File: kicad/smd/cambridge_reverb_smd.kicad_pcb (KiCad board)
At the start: 2 copper layers, 155 x 90 mm, 143 parts, among them IC1 TL072CP, IC2 TL072CP, Q1 MMBF5457, Q2 MMBF5457, T1 reuse / AnTek AS-0524, U1 LM317T

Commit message: SPICE parameter sweeps with committed results; tremolo LFO fix (errata #19); re-route
spice/: six ngspice sweeps next to the fixed-point checks, and run_all.sh now
saves every result table to spice/results/ (committed evidence):
- sweep_preamp_bias: Vd vs R_s for LO/TYP/HI JFET corners (datasheet Idss 1/3/5
  mA). The recovered 2.2k suits a HIGH-Idss part (8.8 V); a typical part wants
  ~1.0k (8.5 V); a 1 mA part cannot reach 8-9 V at any R_s -> errata #15 quantified
- sweep_tonestack: response over the whole pot travel (1 kHz -1.6..-3.3 dB while
  10 kHz falls 14 dB)
- sweep_lfo_speed_recovered: the recovered single-arm Wien LFO oscillates only for
  pot <= ~27k (5 % of travel) at 45-80 Hz, and not at all elsewhere
- sweep_lfo_speed: the fixed network, 10.6 Hz .. 0.60 Hz at constant 0.96 Vpp
- sweep_classa_bias: standing current / heat / THD vs bias (1.4 % -> 0.002 %,
  0.11 -> 0.85 A)
- sweep_pa_headroom: clean power vs rail, mains -10 %..+10 % = 8.9 / 11.7 / 14.8 W

Errata #19 (HIGH): the tremolo LFO did not work as recovered (Wien start condition
gain > 2 + R1/R2 fails with the speed pot in one arm). Built design: dual-gang
250k lin speed pot (one gang per arm, same panel hole), 15k floors, 1 uF timing
caps; POT_SPD_A/B in schematic + BOM = one part. tran_tremolo_lfo.cir aligned
(10.59 Hz at the fast end). Docs: errata, Part 1 s5, Part 2 note, Part 6b, BOM
cross-check, spice README (sweep tables), PCB-NOTES test-point row, README.

Both boards regenerated and re-routed (six settings each; Freerouting is
deterministic per input but placement-sensitive): THT 167/168, 3 starved-thermal
errors (was 166/166 clean); SMD 162/169, DRC clean (was 165/167 + 1 error).
Reports in kicad/reports/, open links listed in PCB-NOTES.

Co-Authored-By: Claude Fable 5.1 <noreply@anthropic.com>
Claude-Session: https://claude.ai/code/session_01Vk8HkvCugxFpQsBPVnNT2H
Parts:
- removed POT_SPD: 500k lin, WirePad_1x03_P2.54mm_D1.2mm
- removed R_lfo1: 33k, R_0805_2012Metric
- added POT_SPD_A: 250k lin dual, WirePad_1x03_P2.54mm_D1.2mm, F.Cu at (50.4, 81.5)
- added POT_SPD_B: 250k lin dual, WirePad_1x03_P2.54mm_D1.2mm, F.Cu at (59.8, 81.5)
- added R_lfo_sh: 15k, R_0805_2012Metric, F.Cu at (48.6, 51.1)
- C_lfo1, C_lfo2: value 100nF -> 1uF; footprint C_1206_3216Metric -> C_1210_3225Metric
- R_lfo_ser: value 10k -> 15k
- moved R_mrb_ser 25.8 mm to (76.0, 14.1)
- moved C_lfo1 16.7 mm to (39.1, 40.4)
- moved C_lfo2 15.8 mm to (33.9, 40.4)
- moved POT_REV 9.43 mm to (90.7, 81.5)
- moved POT_DPT 9.43 mm to (69.3, 81.5)
- moved FS1 9.43 mm to (100.1, 81.5)
- moved LS1 9.43 mm to (117.6, 81.5)
- moved REV1 9.43 mm to (78.7, 81.5)
- moved D_lfo2 5.25 mm to (27.9, 51.3)
- moved R_led 5.25 mm to (60.6, 51.1)
- moved R_lfo_fb1 5.25 mm to (52.6, 51.1)
- moved R_trem1 5.25 mm to (68.6, 51.1)
- moved R_vbt1 5.25 mm to (32.6, 51.1)
- moved R_vbt2 5.25 mm to (36.6, 51.1)
- moved D_lfo1 5.25 mm to (22.5, 51.3)
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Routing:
- net SPK_P: track 65.2 -> 173.9 mm, vias 2 -> 1
- net TONE_OUT: track 118.7 -> 202.0 mm, vias 2 -> 3
- net WMX: track 91.1 -> 159.4 mm, vias 4 -> 2
- net DRMX: track 52.5 -> 116.2 mm, vias 2 -> 4
- net +17V: track 327.0 -> 379.3 mm, vias 1 -> 2
- net LFO_N: track 57.2 -> 109.0 mm, vias 1 -> 3
- net Q2D: track 137.1 -> 94.3 mm, vias 2 -> 4
- net SPD_B: track 0.00 -> 37.4 mm, vias 0 -> 1
- net MRB_OUT: track 93.0 -> 57.1 mm, vias 0 -> 1
- net TREM_OUT: track 118.4 -> 89.0 mm
- net LFO_P: track 71.0 -> 99.0 mm, vias 5 -> 0
- net QRD: track 56.9 -> 84.4 mm, vias 4 -> 2
- net MRB_T: track 72.4 -> 97.3 mm, vias 0 -> 3
- net PREAMP_OUT: track 160.2 -> 135.6 mm
- net WN1: track 77.4 -> 56.4 mm, vias 4 -> 3
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
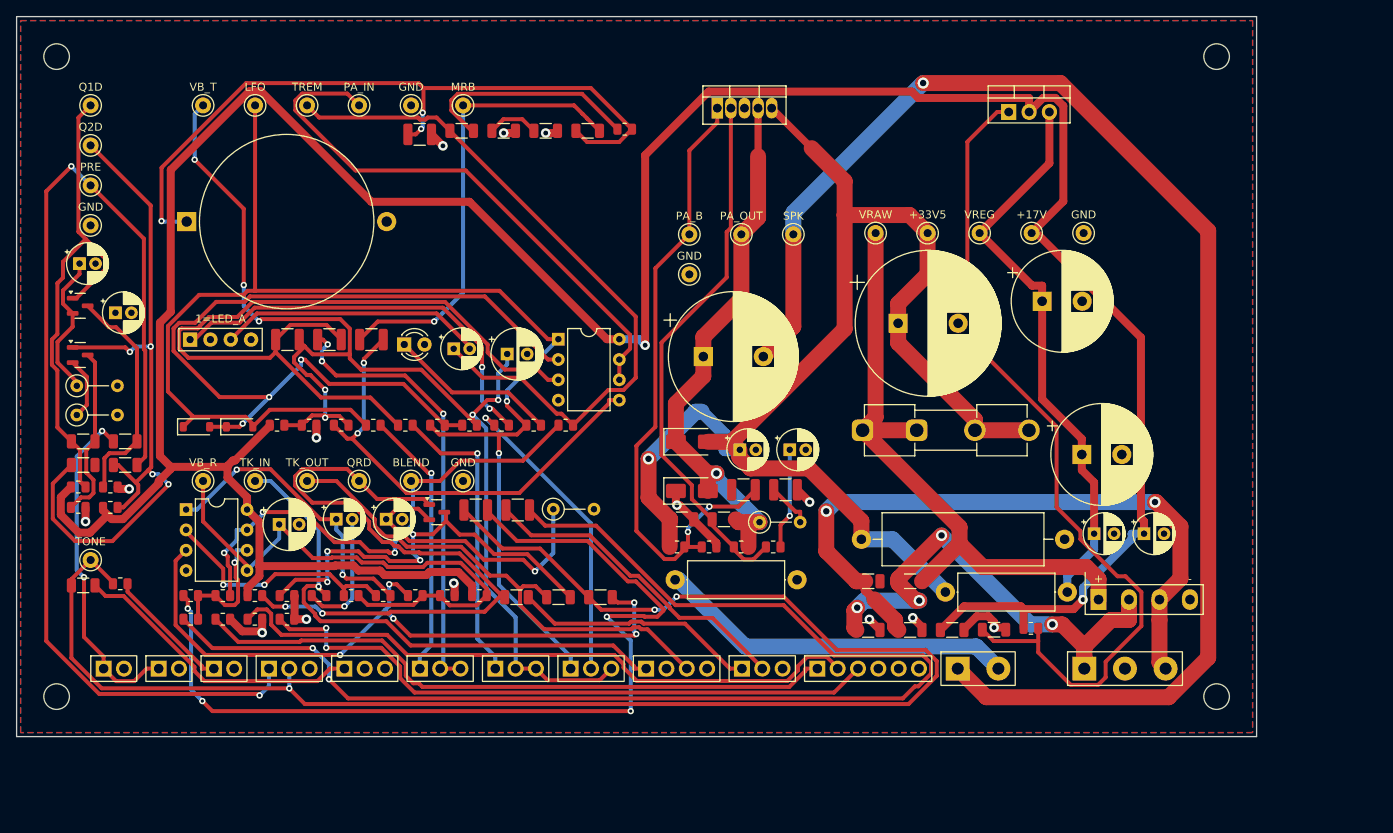
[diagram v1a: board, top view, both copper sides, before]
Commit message: Tone stack: Bass + Treble (passive James) with a switchable mid cut (errata #20)
The panel has Bass and Treble pots, but the design carried a single treble-cut
"Tone" substitute -- and the recovered preamp coupling was the 470 pF chime cap
alone, a 1.3 kHz high-pass that passed no bass at all. Replace both:

- C_cpl_out 1 uF full-band coupling from Q2's drain; C_treble 470 pF becomes a
  bright cap across the top of the volume pot.
- Passive James (Thomas-Vox) Bass/Treble network -- the originals' topology,
  asymmetric, more cut than boost, kept over an active Baxandall so the amp
  keeps its character -- driven by a TL074 (IC3: input buffer, x2 make-up,
  gyrator, output buffer) on its own mid-rail VBIAS_3. Both pots 250k lin in
  the original holes.
- MID CUT toggle for honky pickups: R_mid + a switched series-resonant gyrator
  shunt (1.86 H simulated + 22 nF): -9.6 dB at ~800 Hz, Q ~0.6, flat when off,
  no DC across the switch. SW_MID sits in the original line-reverse switch
  hole -- no new panel holes.
- SPICE: ac_tonestack.cir rewritten rail-aware (all IC3 nodes 8.50 V, noon
  -0.21 dB, notch -9.65 dB at 796 Hz); sweep_tonestack.cir sweeps both pots
  and the switch; results committed.

Generator / placer / router:
- OPAMP14 and SW_SPST symbols, VB_3 / TMK test points (28), BOM rows for IC3,
  the DIP-14 socket, POT_BASS/POT_TREB, SW_MID.
- gen_pcb: tighter profiles (THT 1.2 mm gap / 3.5 mm channels, SMD 0.4 mm),
  overflow repair by moving width between columns, small parts kept in
  schematic order on the shelves, tone/preamp column weighted wider, TP cells
  6x4.5 with the courtyard flush to the cell, input-jack pads down the LEFT
  edge on the 155x90 board (the bottom edge is ~9 mm short for 13 groups),
  keepout rule areas (2 mm edge frame + M3 hole squares) exported to the
  router.
- route_board: refuse a board without its .kicad_pro (a copy routed away from
  the project came back with 0.2 mm tracks and 400 DRC errors); prune
  zero-length segments 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
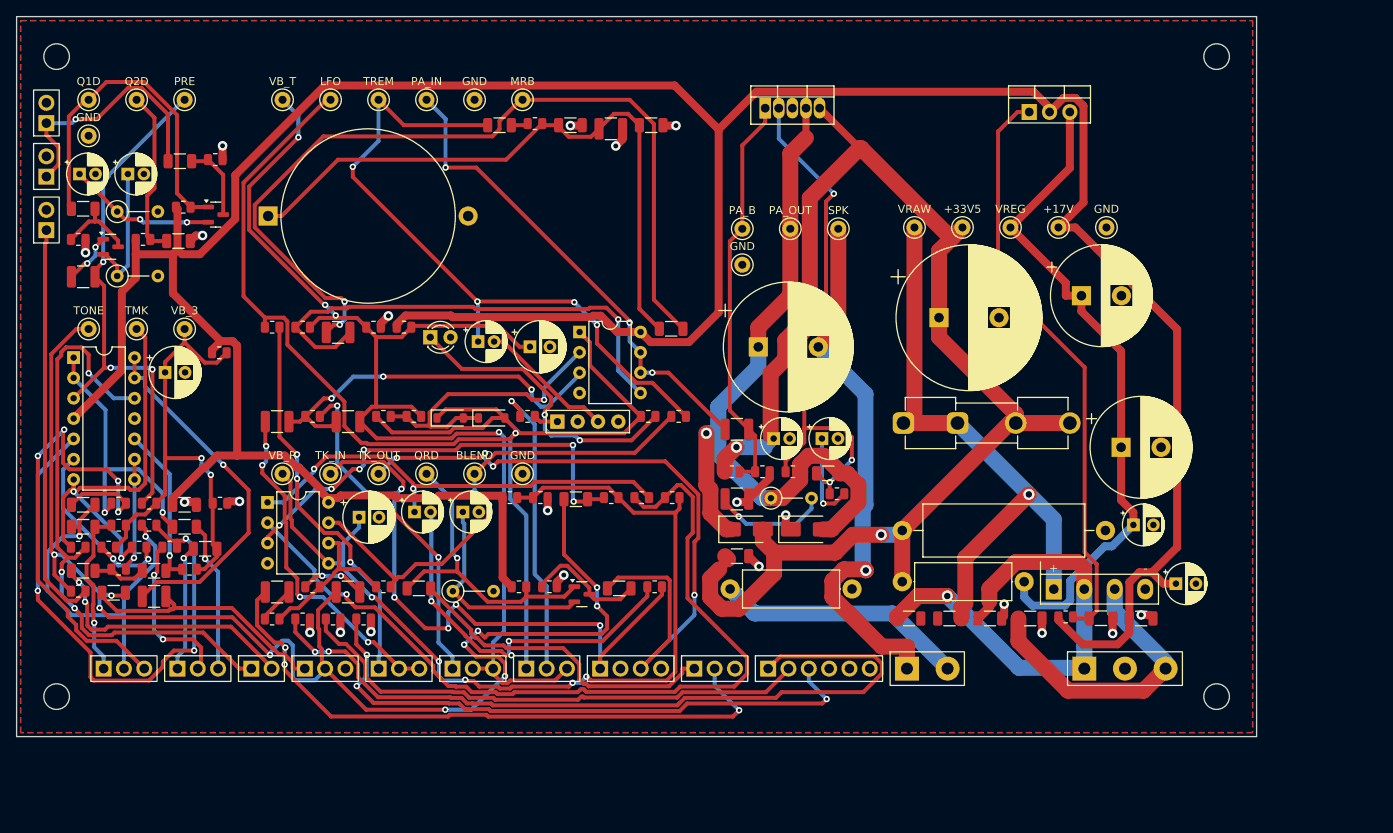
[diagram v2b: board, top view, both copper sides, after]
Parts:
- removed C_cut: 10nF, C_1206_3216Metric
- removed POT_TONE: 100k lin, WirePad_1x03_P2.54mm_D1.2mm
- added C_byp3: 100nF, C_1206_3216Metric, F.Cu at (21.0, 61.0)
- added C_cpl_out: 1uF, C_1210_3225Metric, F.Cu at (8.32, 32.5)
- added C_gg: 1.8nF, C_1206_3216Metric, F.Cu at (17.2, 69.3)
- added C_j1: 22nF, C_1206_3216Metric, F.Cu at (8.32, 61.0)
- added C_j2: 22nF, C_1206_3216Metric, F.Cu at (8.32, 63.8)
- added C_j3: 2.2nF, C_1206_3216Metric, F.Cu at (21.0, 63.8)
- added C_j4: 2.2nF, C_1206_3216Metric, F.Cu at (23.6, 66.5)
- added C_res: 22nF, C_1206_3216Metric, F.Cu at (8.32, 69.3)
- added C_tout: 1uF, C_1210_3225Metric, F.Cu at (17.2, 72.5)
- added C_vb3: 47uF/25V, CP_Radial_D6.3mm_P2.50mm, F.Cu at (18.6, 44.5)
- added IC3: TL074CN, DIP-14_W7.62mm, F.Cu at (7.12, 42.6)
- added POT_BASS: 250k lin, WirePad_1x03_P2.54mm_D1.2mm, F.Cu at (10.9, 81.5)
- added POT_TREB: 250k lin, WirePad_1x03_P2.54mm_D1.2mm, F.Cu at (20.1, 81.5)
- added R_gL: 4.7k, R_0805_2012Metric, F.Cu at (12.8, 69.1)
- added R_gg: 220k, R_0805_2012Metric, F.Cu at (21.6, 69.1)
- added R_inb: 1M, R_0805_2012Metric, F.Cu at (16.6, 60.8)
- added R_j1: 10k, R_0805_2012Metric, F.Cu at (12.8, 60.8)
- added R_j2: 10k, R_0805_2012Metric, F.Cu at (12.8, 63.6)
- added R_j3: 68k, R_0805_2012Metric, F.Cu at (16.6, 63.6)
- added R_j4: 1k, R_0805_2012Metric, F.Cu at (19.1, 66.3)
- added R_mid: 10k, R_0805_2012Metric, F.Cu at (7.71, 66.3)
- added R_mk1: 10k, R_0805_2012Metric, F.Cu at (15.3, 66.3)
- added R_mk2: 10k, R_0805_2012Metric, F.Cu at (11.5, 66.3)
- added R_vb31: 100k, R_0805_2012Metric, F.Cu at (25.3, 42.0)
- added R_vb32: 100k, R_0805_2012Metric, F.Cu at (25.4, 60.8)
- added SW_MID: MID CUT, WirePad_1x02_P2.54mm_D1.2mm, F.Cu at (29.3, 81.5)
- added TP_MK_OUT: TMK, TestPoint_THT_D2.0mm_Label, F.Cu at (15.0, 39.0)
- added TP_VBIAS_3: VB_3, TestPoint_THT_D2.0mm_Label, F.Cu at (21.0, 39.0)
- moved J_IN1 68.6 mm to (3.73, 13.3), turned to 90 degrees
- moved J_IN2 63.1 mm to (3.73, 20.0), turned to 90 degrees
- moved J_IN3 58.7 mm to (3.73, 26.7), turned to 90 degrees
- moved VTL1 47.0 mm to (67.6, 50.6)
- moved R_g1 43.0 mm to (24.8, 17.9)
- moved R_drv3 42.0 mm to (79.8, 71.3)
- moved R_drv2 42.0 mm to (82.0, 60.1)
- moved R_d1 37.4 mm to (20.8, 23.8)
- moved C_in_pre 35.7 mm to (20.4, 18.1)
- moved R_drv1 34.6 mm to (78.1, 60.1)
- moved R_d2 33.7 mm to (15.8, 27.9)
- moved R_g2 33.5 mm to (7.71, 27.9)
- moved R_rec1 33.0 mm to (62.8, 71.3)
- moved R_rec_bias 32.8 mm to (66.6, 71.3)
- moved C_wetmix 31.8 mm to (32.6, 71.9)
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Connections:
- C_treble pad 1: Q2D -> VOLTOP
- C_treble pad 2: PREAMP_OUT -> TONE_OUT
- POT_VOL pad 1: PREAMP_OUT -> VOLTOP
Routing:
- net WMX: track 159.4 -> 4.62 mm, vias 2 -> 0
- net DRMX: track 116.2 -> 8.21 mm, vias 4 -> 2
- net SPK_P: track 173.9 -> 68.0 mm
- net MID: track 0.00 -> 76.3 mm, vias 0 -> 3
- net R_INV: track 30.7 -> 106.4 mm, vias 2 -> 1
- net LFO_N: track 109.0 -> 36.9 mm, vias 3 -> 1
- net JOUT: track 0.00 -> 69.4 mm, vias 0 -> 3
- net PREAMP_OUT: track 135.6 -> 67.4 mm, vias 2 -> 3
- net Q2D: track 94.3 -> 27.6 mm, vias 4 -> 2
- net JA: track 0.00 -> 64.2 mm, vias 0 -> 4
- net VBIAS_3: track 0.00 -> 59.1 mm, vias 0 -> 2
- net MK_OUT: track 0.00 -> 53.2 mm, vias 0 -> 2
- net LFO_P: track 99.0 -> 47.2 mm, vias 0 -> 3
- net MRB_OUT: track 57.1 -> 107.4 mm, vias 1 -> 2
- net VLED: track 51.6 -> 3.09 mm, vias 2 -> 0
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
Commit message: Noise, hum, crosstalk and thermal models; three design fixes; JLCPCB rules and cost
New models (docs/06c, spice/): a .noise run of the whole front end including the
LM317's own rail noise, the rail-ripple paths to the speaker, a vactrol-level tremolo
depth model, an electro-thermal LM1875 ladder, and a geometric crosstalk audit of the
routed boards (kicad/gen/crosstalk_audit.py). They found three defects:

- Errata #21 (hum + hiss): the LM1875 bias divider had no bypass (+4 dB ripple to
  speaker, 0.4 Vrms of 100 Hz at idle) and the LM317's 0.5 mV of noise reached the
  0 dB-PSRR JFET stages (23 dB above their floor, SNR 34 dB). Fixed with C_bref +
  R_bias3 on the power amp, C_adj on the regulator, and an RC-decoupled +17V_PRE rail
  for Q1/Q2/Q_rec: hum 408 mV -> 0.3 mV, EIN 37 -> 2.7 uV, SNR 34 -> 57 dB.
- Errata #22 (tremolo depth 1.7 dB): the vactrol LED was returned to ground from a
  mid-rail LFO -> 7 mA DC, a fixed -20 dB pad. LED limiter (2 V swing, LED_rate is one
  limiter LED) + Q_trem 2N3904/MMBT3904 emitter follower AC-coupled from the depth
  pot -> 15 dB depth, 0.8 dB insertion loss.
- Errata #23 (fab): stock TO-92 and the LM1875 footprint were under JLCPCB's 0.18 mm
  annular-ring minimum -> TO-92_Inline_Wide and 1.5 mm LM1875 pads; both .kicad_pro
  carry JLC's 2-layer limits as DRC constraints. Cost: all SMD caps 1206 (basic
  library), "(opt)" MRB caps DNP, gyrator on E24 values (same 1.86 H): 7 -> 2
  extended part types, ~$32 -> ~$17 assembly for five boards (kicad/gen/jlc_cost.py);
  three fiducials on the SMD board.

Crosstalk -> two routing rules (.kicad_dru: HighCurrent 0.6/0.4 mm and TankDrive
1.2/0.8 mm from signal copper, THT/SMD) that route_board.py also hands the router as
class clearances; keepout rule areas along the edge and around the mounting holes.
Thermal: Part 5's <= 2.5 K/W heatsink confirmed with numbers (Tj 97 C at 40 C ambient,
worst-case sine; 8-10 K/W clip-ons reach shutdown).

Placer: short parts stack beside tall ones i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
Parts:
- removed the C_cpl_out at (8.32, 32.5)
- removed the C_drymix at (41.4, 71.9)
- removed the C_in_pa at (90.0, 51.6)
- removed the C_obuf_in at (40.2, 39.5)
- removed the C_tout at (17.2, 72.5)
- removed the C_wetmix at (32.6, 71.9)
- removed the C_zobel at (90.0, 60.3)
- removed D_lfo1, D_lfo2: 1N4148, D_SOD-123
- removed R_led: 1k, R_0805_2012Metric
- removed R_led_diag: 2.2k, R_0805_2012Metric
- added C_adj: 10uF/25V, CP_Radial_D5.0mm_P2.00mm, F.Cu at (138.9, 70.9)
- added C_bref: 100uF/25V, CP_Radial_D6.3mm_P2.50mm, F.Cu at (92.4, 53.4)
- added C_cpl_out: 1uF, C_1206_3216Metric, F.Cu at (8.32, 31.5)
- added C_drv: 100uF/25V, CP_Radial_D6.3mm_P2.50mm, F.Cu at (70.1, 41.3)
- added C_drymix: 1uF, C_1206_3216Metric, F.Cu at (43.4, 68.0)
- added C_in_pa: 1uF, C_1206_3216Metric, F.Cu at (80.4, 58.4)
- added C_obuf_in: 1uF, C_1206_3216Metric, F.Cu at (44.7, 41.4)
- added C_pre: 220uF/25V, CP_Radial_D6.3mm_P2.50mm, F.Cu at (134.0, 64.2)
- added C_tout: 1uF, C_1206_3216Metric, F.Cu at (21.0, 62.3)
- added C_wetmix: 1uF, C_1206_3216Metric, F.Cu at (34.6, 68.0)
- added C_zobel: 100nF, C_1206_3216Metric, F.Cu at (80.4, 61.1)
- added FID1: Fiducial_1mm_Mask2mm, Fiducial_1mm_Mask2mm, F.Cu at (12.0, 4.00)
- added FID2: Fiducial_1mm_Mask2mm, Fiducial_1mm_Mask2mm, F.Cu at (143.0, 4.00)
- added FID3: Fiducial_1mm_Mask2mm, Fiducial_1mm_Mask2mm, F.Cu at (143.0, 86.0)
- added LED_lim: 3mm red, LED_D3.0mm, F.Cu at (52.4, 40.1)
- added Q_trem: 2N3904, SOT-23_MMBT3904_as_EBC, F.Cu at (49.4, 47.0)
- added R_b1: 180k, R_0805_2012Metric, F.Cu at (41.6, 46.1)
- added R_b2: 10k, R_0805_2012Metric, F.Cu at (45.4, 46.1)
- added R_bias3: 22k, R_0805_2012Metric, F.Cu at (92.4, 58.2)
- added R_c: 100R, R_0805_2012Metric, F.Cu at (57.3, 46.1)
- added R_e: 470R, R_0805_2012Metric, F.Cu at (53.5, 46.1)
- added R_pre: 100R, R_0805_2012Metric, F.Cu at (133.7, 75.0)
- C_gg: value 1.8nF -> 2.2nF
- C_lfo1, C_lfo2, C_mrb_450: footprint C_1210_3225Metric -> C_1206_3216Metric
- R_gg: value 220k -> 180k
- moved IC2 25.8 mm to (66.2, 14.0)
- moved C_j1 25.1 mm to (26.0, 43.1)
- moved C_j2 25.1 mm to (26.0, 45.9)
- moved R_j1 24.2 mm to (26.0, 40.5)
- moved C_mrb_out 22.9 mm to (62.4, 26.9)
- moved R_j2 20.1 mm to (26.0, 48.4)
- moved C_mrb_750 20.0 mm to (62.4, 24.2)
- moved C_treble 17.0 mm to (26.0, 62.3)
- moved R_j3 15.9 mm to (26.0, 50.8)
- moved C_vbt 15.0 mm to (68.8, 27.0)
- moved C_byp2 14.7 mm to (79.9, 52.7)
- moved C_gain 14.7 mm to (86.0, 52.7)
- moved R_drv3 14.4 mm to (69.3, 61.3)
- moved C_mrb_450 14.0 mm to (62.4, 21.4)
- moved C_lfo1 13.6 mm to (39.6, 39.0)
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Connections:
- LED_rate pad 1: DLED -> LFO_OUT
- LED_rate pad 2: GND -> LFO_N
- R_bias1 pad 2: PA_BIAS -> PA_BREF
- R_bias2 pad 1: PA_BIAS -> PA_BREF
- R_d1 pad 1: +17V -> +17V_PRE
- R_d2 pad 1: +17V -> +17V_PRE
- R_rec1 pad 1: +17V -> +17V_PRE
- VTL1 pad 2: GND -> QC
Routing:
- net +17V_PRE: track 0.00 -> 289.9 mm, vias 0 -> 7
- net AC1: track 58.8 -> 253.9 mm, vias 1 -> 3
- net LFO_OUT: track 166.6 -> 104.8 mm, vias 1 -> 0
- net R_INV: track 106.4 -> 45.4 mm, vias 1 -> 3
- net MRB_OUT: track 107.4 -> 48.3 mm, vias 2 -> 0
- net TKDRV: track 46.8 -> 0.00 mm, vias 3 -> 0
- net VBIAS_R: track 116.4 -> 75.1 mm, vias 5 -> 2
- net PA_GAIN: track 11.3 -> 51.7 mm, vias 1 -> 3
- net DLED: track 38.2 -> 0.00 mm, vias 2 -> 0
- net FS_REV: track 97.9 -> 61.1 mm, vias 2 -> 0
- net QB: track 0.00 -> 35.4 mm
- net MRB_T: track 80.2 -> 45.0 mm, vias 0 -> 1
- net PA_OUT: track 95.7 -> 129.5 mm, vias 1 -> 2
- net TONE_OUT: track 168.8 -> 138.3 mm, vias 10 -> 5
- net +17V: track 418.6 -> 388.4 mm
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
